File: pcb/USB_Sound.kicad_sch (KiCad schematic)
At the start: 8 parts, among them IC1 PCM2706, J1 USB4500-03-0-A_REVA, U8 FSUSB42MUX, Y1 Crystal

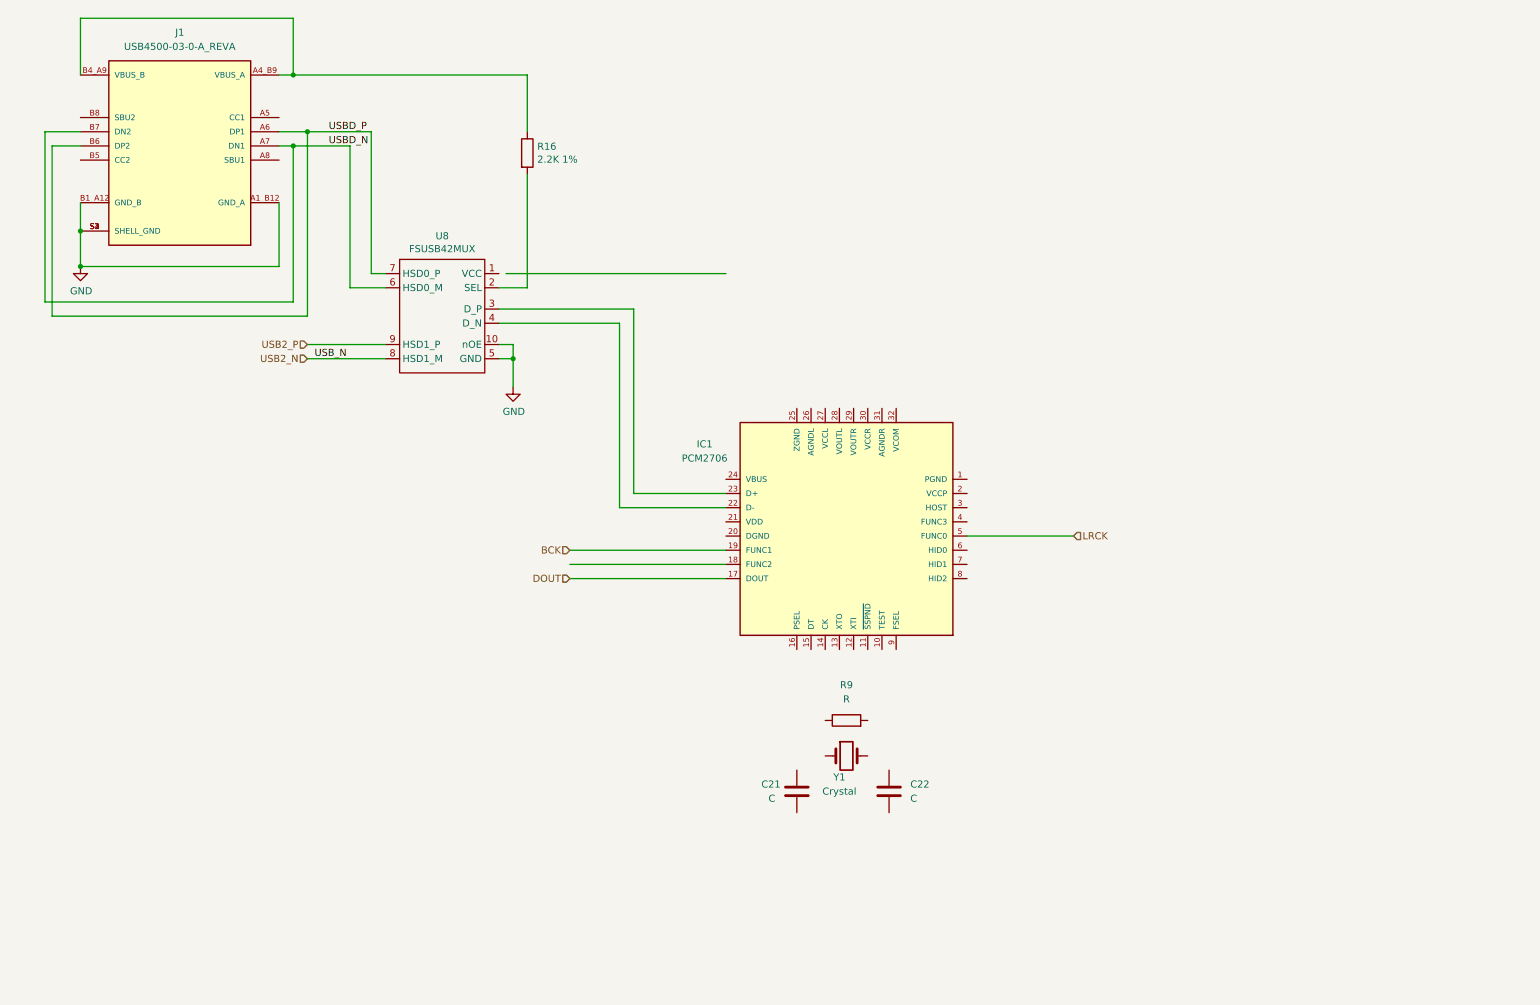
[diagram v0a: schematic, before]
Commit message: - USB sound wired
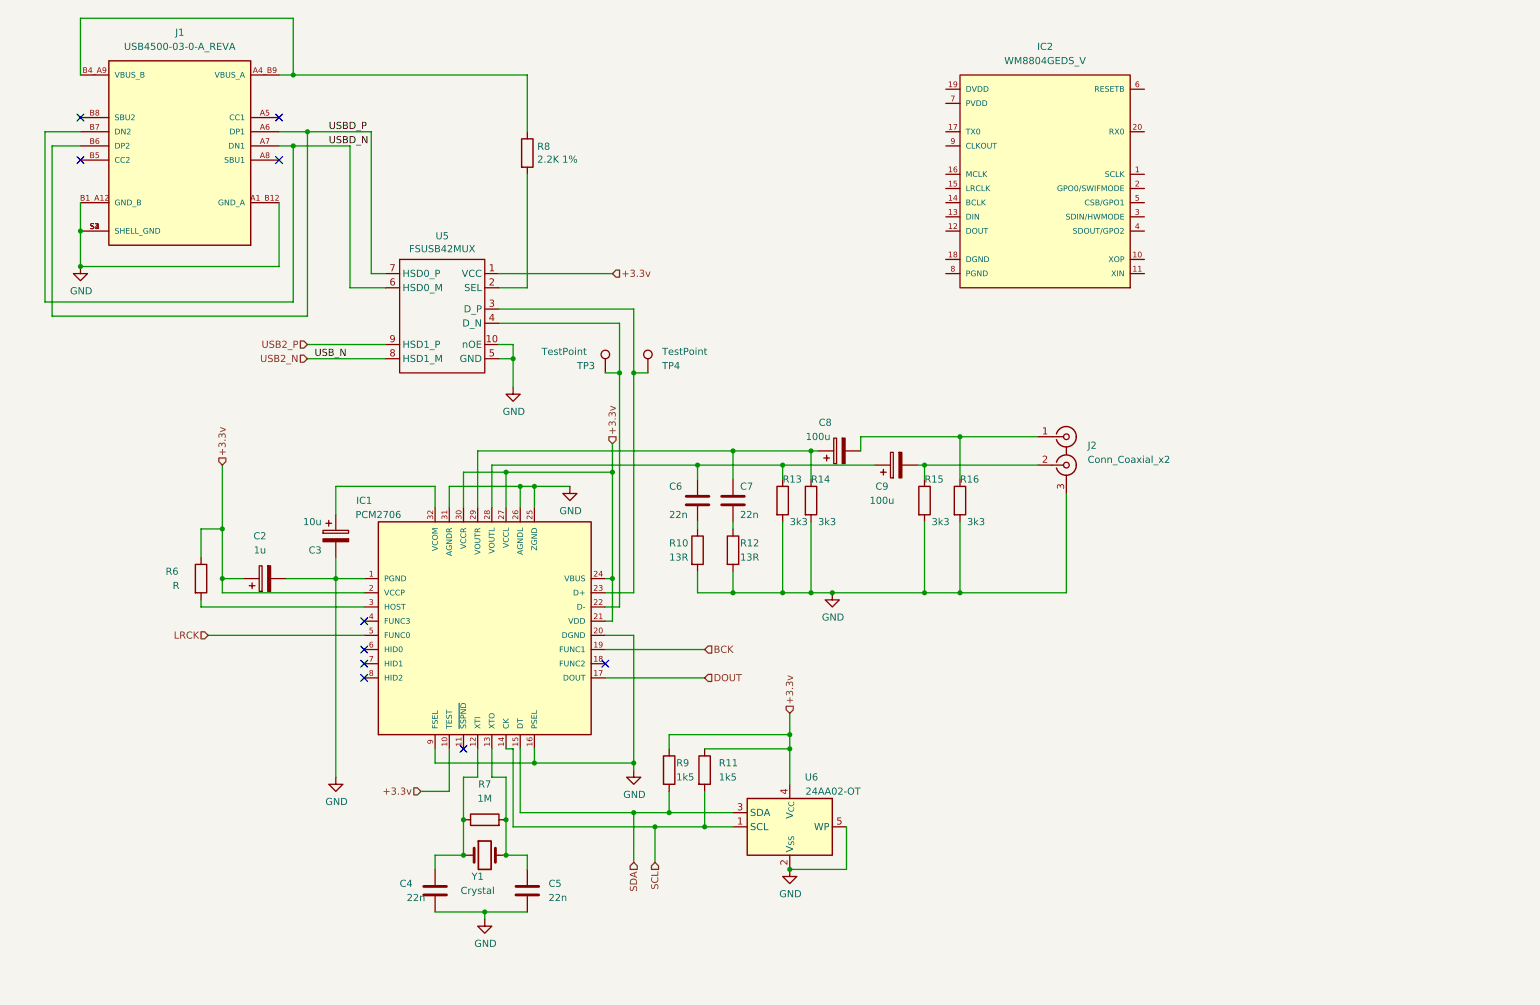
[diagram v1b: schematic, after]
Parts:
- added C2: 1u, symbol Device:C_Polarized
- added C3: 10u, symbol Device:C_Polarized
- added C6, C7: 22n, symbol Device:C
- added C8, C9: 100u, symbol Device:C_Polarized
- added IC2: WM8804GEDS_V, Footprints:SOP65P780X200-20N, symbol WM8804GEDS_V:WM8804GEDS_V
- added J2: Conn_Coaxial_x2, symbol Connector:Conn_Coaxial_x2
- added R10, R12: 13R, symbol Device:R
- added R11, R9: 1k5, symbol Device:R
- added R13, R14, R15, R16: 3k3, symbol Device:R
- added R6: R, symbol Device:R
- added TP3, TP4: TestPoint, TestPoint:TestPoint_Bridge_Pitch2.54mm_Drill1.0mm, symbol Connector:TestPoint
- added U6: 24AA02-OT, Package_TO_SOT_SMD:SOT-23-5, symbol Memory_EEPROM:24AA02-OT
- C4: renamed from C21; value C -> 22n
- C5: renamed from C22; value C -> 22n
- R7: renamed from R9; value R -> 1M
- renumbered R16 to R8, U8 to U5
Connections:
- net GND: now also C4.2, C5.2, IC1.1 (PGND), IC1.16 (PSEL), IC1.20 (DGND), IC1.25 (ZGND), IC1.26 (AGNDL), IC1.31 (AGNDR), IC1.9 (FSEL), C2.2, C3.2, J2.3 (EXT), R10.2, R12.2, R13.2, R14.2, R15.2, R16.2, U6.2 (V_{SS}), U6.5 (WP)
- net at C5.1: now also IC1.13 (XTO), R7.2, Y1.2
- net +3.3v: now reaches IC1.10 (TEST)
- net +3.3v: now also IC1.2 (VCCP), IC1.21 (VDD), IC1.24 (VBUS), IC1.27 (VCCL), IC1.30 (VCCR), U5.1 (VCC), C2.1, R11.1, R6.1, R9.1, U6.4 (V_{CC})
- net at IC1.12 (XTI): now also C4.1, R7.1, Y1.1
- net SCL: now reaches IC1.14 (CK)
- net SCL: now also R11.2, U6.1 (SCL)
- net SDA: now reaches IC1.15 (DT)
- net SDA: now also R9.2, U6.3 (SDA)
- net at IC1.22 (D-), U5.4 (D_N): now also TP3.1
- net at IC1.23 (D+), U5.3 (D_P): now also TP4.1
- net at IC1.28 (VOUTL): now also C6.1, C9.1, R13.1
- net at IC1.29 (VOUTR): now also C7.1, C8.1, R14.1
- net at IC1.3 (HOST): now also R6.2
- net at IC1.32 (VCOM): now also C3.1
- new net: C9.2, J2.2 (IN2), R15.1
- new net: C8.2, J2.1 (IN1), R16.1
- new net: C6.2, R10.1
- new net: C7.2, R12.1
- no-connect marks 0 -> 10
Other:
- moved on the sheet: C4, C5, IC1, R7, Y1

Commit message: WM8804 via i2c
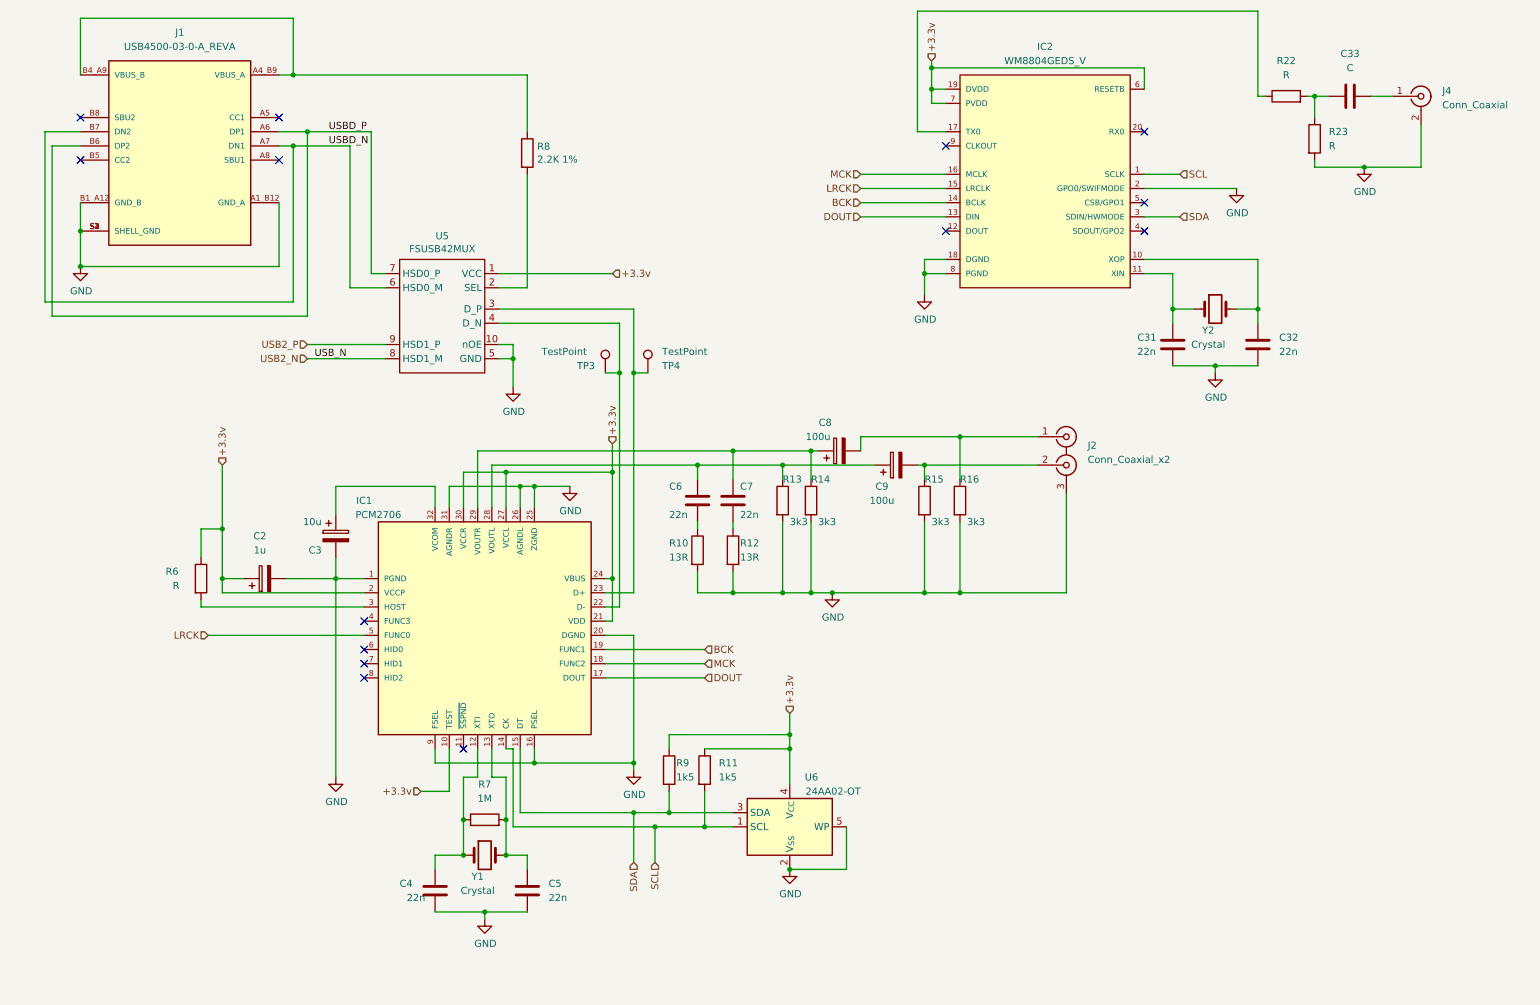
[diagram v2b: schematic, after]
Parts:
- added C31, C32: 22n, symbol Device:C
- added C33: C, symbol Device:C
- added J4: Conn_Coaxial, symbol Connector:Conn_Coaxial
- added R22, R23: R, symbol Device:R
- added Y2: Crystal, symbol Device:Crystal
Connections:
- net +3.3v: now also IC2.19 (DVDD), IC2.6 (RESETB), IC2.7 (PVDD)
- net BCK: now also IC2.14 (BCLK)
- net DOUT: now also IC2.13 (DIN)
- net GND: now also IC2.18 (DGND), IC2.2 (GPO0/SWIFMODE), IC2.8 (PGND), C31.2, C32.2, J4.2 (Ext), R23.2
- net LRCK: now also IC2.15 (LRCLK)
- net SCL: now also IC2.1 (SCLK)
- net SDA: now also IC2.3 (SDIN/HWMODE)
- net at IC2.10 (XOP): now also C32.1, Y2.2
- net at IC2.11 (XIN): now also C31.1, Y2.1
- net MCK: now reaches IC2.16 (MCLK)
- net MCK: now also IC1.18 (FUNC2)
- net at IC2.17 (TX0): now also R22.1
- new net: C33.1, R22.2, R23.1
- new net: C33.2, J4.1 (In)
- no-connect marks 10 -> 14

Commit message: - work in progress
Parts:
- removed C31, C32: 22n, symbol Device:C
- removed C33: C, symbol Device:C
- removed IC2: WM8804GEDS_V, Footprints:SOP65P780X200-20N, symbol WM8804GEDS_V:WM8804GEDS_V
- removed J4: Conn_Coaxial, symbol Connector:Conn_Coaxial
- removed R22, R23: R, symbol Device:R
- removed Y2: Crystal, symbol Device:Crystal
- added JP4: LRCK, symbol Jumper:SolderJumper_2_Open
- added JP5: BCK, symbol Jumper:SolderJumper_2_Open
- added JP6: MCK, symbol Jumper:SolderJumper_2_Open
- added JP7: D, symbol Jumper:SolderJumper_2_Open
- added TP10: Host, TestPoint:TestPoint_Bridge_Pitch2.54mm_Drill1.0mm, symbol Connector:TestPoint
- added TP3, TP4: TestPoint, TestPoint:TestPoint_Bridge_Pitch2.54mm_Drill1.0mm, symbol Connector:TestPoint
- R6: value R -> 1k
- renumbered TP3 to TP5, TP4 to TP6
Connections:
- net SCL: now also TP4.1
- net SDA: now also TP3.1
- net at IC1.3 (HOST), R6.2: now also TP10.1
- net BCK: no longer names the net of IC1.19 (FUNC1)
- net BCK: now also JP5.1 (A)
- net DOUT: no longer names the net of IC1.17 (DOUT)
- net DOUT: now also JP7.1 (A)
- net LRCK: no longer names the net of IC1.5 (FUNC0)
- net LRCK: now also JP4.2 (B)
- net MCK: no longer names the net of IC1.18 (FUNC2)
- net MCK: now also JP6.1 (A)
- new net I2S.BCK: JP5.2 (B)
- new net I2S.LRCK: JP4.1 (A)
- new net I2S.MCK: JP6.2 (B)
- no-connect marks 14 -> 9
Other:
- moved on the sheet: C4, C5, R11, R7, R9, U6, Y1
